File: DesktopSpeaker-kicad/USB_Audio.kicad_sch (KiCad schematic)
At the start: 20 parts, among them U2 PCM2902CDBR, Y170 12MHz

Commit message: Replace SWD header with TC2030-IDC and 4-pin header; set USB audio crystal caps and resistor parts
Co-Authored-By: Claude Sonnet 5.5 <noreply@anthropic.com>
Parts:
- C177, C178: value 22pF -> 33pF; LCSC C1653 -> C1663; MPN CL10C220JB8NNNC -> CL10C330JB8NNNC
- R170: LCSC (none) -> C112307
- R171, R172: LCSC (none) -> C107701

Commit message: Capture Source_Select_ADC sheet (PCM1862, 3V3_AUDIO LDO, codec load switch)
Co-Authored-By: Claude Sonnet 5.5 <noreply@anthropic.com>
Claude-Session: https://claude.ai/code/session_01N5RHheWSjDFDPbKVD5YVeJ
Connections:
- net 5V_LOGIC renamed 5V_CODEC
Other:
- note added: "Codec is powered only when CODEC_PWR_EN (U23) and 5V_LOGIC are on: D+ pull-up (R173 to VDDI) = USB attach. Do not enable CODEC_PWR_EN on DCP/unknown sources."
- note added: "Supply: 5V_CODEC (U23 load switch from 5V_LOGIC, 4.60-5.06 V worst case) feeds VBUS through 2.2R/1uF. DS range 4.35-5.25 V, 56 mA typ / 67 mA max, 250 uA suspend."
- note removed: "Codec is powered only when 5V_LOGIC_EN is high: D+ pull-up (R173 to VDDI) = USB attach. Do not enable on DCP/unknown sources."
- note removed: "Supply: 5V_LOGIC (U14 TPS63802, 4.60-5.06 V worst case) feeds VBUS through 2.2R/1uF. DS range 4.35-5.25 V, 56 mA typ / 67 mA max, 250 uA suspend."
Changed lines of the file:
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@@
 (wire (pts (xy 93.98 68.58) (xy 90.17 68.58)) (stroke (width 0) (type default)))
 (wire (pts (xy 82.55 68.58) (xy 57 68.58)) (stroke (width 0) (type default)))
-(hierarchical_label "5V_LOGIC" (shape input) (at 57 68.58 0) (effects (font (size 1.0 1.0)) (justify left bottom)))
+(hierarchical_label "5V_CODEC" (shape input) (at 57 68.58 0) (effects (font (size 1.0 1.0)) (justify left bottom)))
 (symbol (lib_id "PD_R:PD_R") (at 86.36 68.58 90) (unit 1) (exclude_from_sim no) (in_bom yes) (on_board yes) (dnp no) (property "Reference" "R170" (at 86.36 64.38 270) (effects (font (size 1.27 1.27)) )) (property "Value" "2.2" (at 86.36 65.98 270) (effects (font (size 1.27 1.27)) )) (property "Footprint" "DesktopSpeaker:PD_R_0603" (at 86.36 68.58 0) (hide yes) (effects (font (size 1.27 1.27)))) (property "MPN" "RC0603FR-072R2L" (at 86.36 68.58 0) (hide yes) (effects (font (size 1.27 1.27)))) (property "Manufacturer" "YAGEO" (at 86.36 68.58 0) (hide yes) (effects (font (size 1 1)))) (property "LCSC" "C112307" (at 86.36 68.58 0) (hide yes) (effects (font (size 1 1)))) (pin "1") (pin "2") (instances (project "DesktopSpeaker" (path "/feda53ed-537d-4f88-9436-c6075776255b/54e0bbc5-df7c-4047-acfa-4732ab128bc4" (reference "R170") (unit 1)))))
 (symbol (lib_id "PD_C:PD_C") (at 93.98 72.39 0) (unit 1) (exclude_from_sim no) (in_bom yes) (on_board yes) (dnp no) (property "Reference" "C170" (at 95.25 71.12 0) (effects (font (size 1.27 1.27)) (justify left))) (property "Value" "1uF" (at 95.25 73.66 0) (effects (font (size 1.27 1.27)) (justify left))) (property "Footprint" "DesktopSpeaker:PD_C_0805" (at 93.98 72.39 0) (hide yes) (effects (font (size 1.27 1.27)))) (property "MPN" "CL21B105KBFNNNE" (at 93.98 72.39 0) (hide yes) (effects (font (size 1.27 1.27)))) (property "Manufacturer" "Samsung Electro-Mechanics" (at 93.98 72.39 0) (hide yes) (effects (font (size 1 1)))) (property "LCSC" "C28323" (at 93.98 72.39 0) (hide yes) (effects (font (size 1 1)))) (pin "1") (pin "2") (instances (project "DesktopSpeaker" (path "/feda53ed-537d-4f88-9436-c6075776255b/54e0bbc5-df7c-4047-acfa-4732ab128bc4" (reference "C170") (unit 1)))))
@@
 (symbol (lib_id "power:GND") (at 180.34 137.16 0) (unit 1) (exclude_from_sim no) (in_bom no) (on_board no) (dnp no) (property "Reference" "#PWR713" (at 180.34 140.97 0) (effects (font (size 1.27 1.27)) (hide yes))) (property "Value" "GND" (at 180.34 142.24 0) (effects (font (size 1.27 1.27)) (hide yes))) (pin "1") (instances (project "DesktopSpeaker" (path "/feda53ed-537d-4f88-9436-c6075776255b/54e0bbc5-df7c-4047-acfa-4732ab128bc4" (reference "#PWR713") (unit 1)))))
 (hierarchical_label "USB_AUDIO_R" (shape output) (at 215.9 129.54 0) (effects (font (size 1.0 1.0)) (justify right bottom)))
-(text "Supply: 5V_LOGIC (U14 TPS63802, 4.60-5.06 V worst case) feeds VBUS through 2.2R/1uF. DS range 4.35-5.25 V, 56 mA typ / 67 mA max, 250 uA suspend." (at 57 53.6 0) (effects (font (size 1 1)) (justify left bottom)))
-(text "Codec is powered only when 5V_LOGIC_EN is high: D+ pull-up (R173 to VDDI) = USB attach. Do not enable on DCP/unknown sources." (at 57 56.1 0) (effects (font (size 1 1)) (justify left bottom)))
+(text "Supply: 5V_CODEC (U23 load switch from 5V_LOGIC, 4.60-5.06 V worst case) feeds VBUS through 2.2R/1uF. DS range 4.35-5.25 V, 56 mA typ / 67 mA max, 250 uA suspend." (at 57 53.6 0) (effects (font (size 1 1)) (justify left bottom)))
+(text "Codec is powered only when CODEC_PWR_EN (U23) and 5V_LOGIC are on: D+ pull-up (R173 to VDDI) = USB attach. Do not enable CODEC_PWR_EN on DCP/unknown sources." (at 57 56.1 0) (effects (font (size 1 1)) (justify left bottom)))
 (text "SEL0/SEL1 = high (VDDI). HID0-2, DIN, VINL/R unused. SSPND (suspend flag, active low) reserved for a later MCU input." (at 57 58.6 0) (effects (font (size 1 1)) (justify left bottom)))
 (text "USB_DP/USB_DN come from J1 via D1 (root). Later source-detect mux goes between those root nets and these ports." (at 57 61.1 0) (effects (font (size 1 1)) (justify left bottom)))

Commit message: Repackage passives to 0402/0805 hand-solder footprints; update BOM and flags
Co-Authored-By: Claude Sonnet 5.5 <noreply@anthropic.com>
Claude-Session: https://claude.ai/code/session_01N5RHheWSjDFDPbKVD5YVeJ
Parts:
- C170, C171, C172, C173, C174: footprint DesktopSpeaker:PD_C_0805 -> DesktopSpeaker:C_0402_1005Metric_Pad0.74x0.62mm_HandSolder; LCSC C28323 -> C29266; MPN CL21B105KBFNNNE -> CL05A105KO5NNNC
- C175, C176: footprint DesktopSpeaker:PD_C_0805 -> DesktopSpeaker:C_0805_2012Metric_Pad1.18x1.45mm_HandSolder
- C177, C178: footprint DesktopSpeaker:PD_C_0603 -> DesktopSpeaker:C_0402_1005Metric_Pad0.74x0.62mm_HandSolder; LCSC C1663 -> (none); MPN CL10C330JB8NNNC -> GRM1555C1H330JA01D; Manufacturer Samsung Electro-Mechanics -> Murata
- C186, C187: footprint DesktopSpeaker:PD_C_1206 -> DesktopSpeaker:C_0805_2012Metric_Pad1.18x1.45mm_HandSolder; LCSC C51205 -> (none); MPN CL31B475KBHNNNE -> CL21A475KAQNNNE
- R170: footprint DesktopSpeaker:PD_R_0603 -> DesktopSpeaker:R_0402_1005Metric_Pad0.72x0.64mm_HandSolder; LCSC C112307 -> (none); MPN RC0603FR-072R2L -> RC0402FR-072R2L; Manufacturer YAGEO -> Yageo
- R171, R172: footprint DesktopSpeaker:PD_R_0603 -> DesktopSpeaker:R_0402_1005Metric_Pad0.72x0.64mm_HandSolder; LCSC C107701 -> (none); MPN RC0603FR-0722RL -> RC0402FR-0722RL; Manufacturer YAGEO -> Yageo
- R173: footprint DesktopSpeaker:PD_R_0603 -> DesktopSpeaker:R_0402_1005Metric_Pad0.72x0.64mm_HandSolder; LCSC C114668 -> C114759; MPN RC0603FR-071K5L -> RC0402FR-071K5L; Manufacturer YAGEO -> Yageo
- R174: footprint DesktopSpeaker:PD_R_0603 -> DesktopSpeaker:R_0402_1005Metric_Pad0.72x0.64mm_HandSolder; LCSC C105578 -> (none); MPN RC0603FR-071ML -> RC0402FR-071ML; Manufacturer YAGEO -> Yageo
- R175, R176: footprint DesktopSpeaker:PD_R_0603 -> DesktopSpeaker:R_0402_1005Metric_Pad0.72x0.64mm_HandSolder; LCSC C14675 -> C60491; MPN RC0603FR-07100KL -> RC0402FR-07100KL; Manufacturer YAGEO -> Yageo

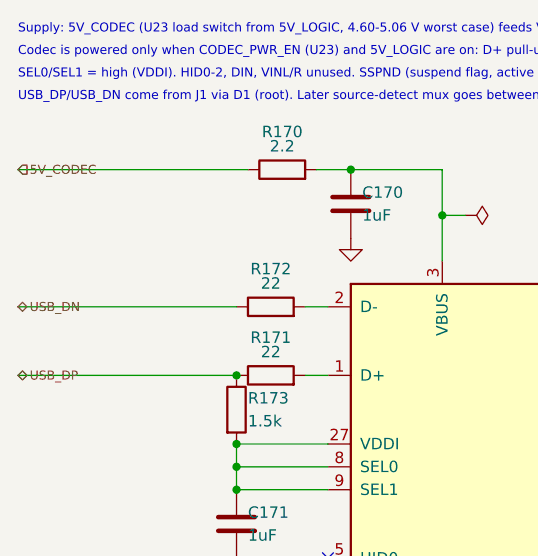
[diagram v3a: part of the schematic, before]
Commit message: Routing R6a-R6m adopted into project board; ERC cleanup, MCU pin swaps, C241 2.2uF, SW100 footprint fix, reviews and helpers
Co-Authored-By: Claude Sonnet 5.5 <noreply@anthropic.com>
Claude-Session: https://claude.ai/code/session_016fe4xPJbEE2SjGafuyNLjb
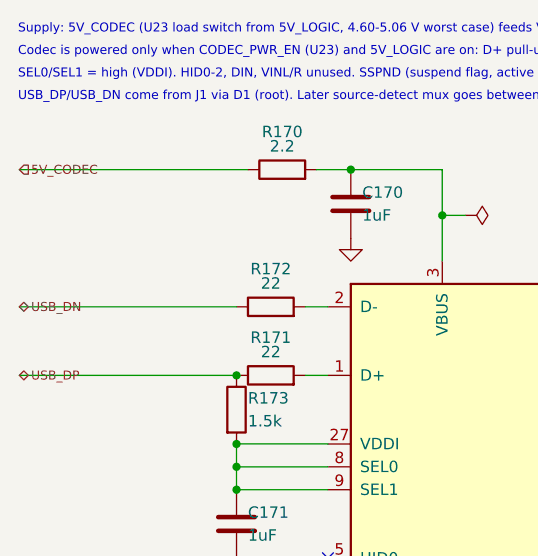
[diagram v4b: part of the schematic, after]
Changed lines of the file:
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@@
 (junction (at 93.98 68.58) (diameter 0) (color 0 0 0 0))
 (wire (pts (xy 93.98 68.58) (xy 90.17 68.58)) (stroke (width 0) (type default)))
-(wire (pts (xy 82.55 68.58) (xy 57 68.58)) (stroke (width 0) (type default)))
-(hierarchical_label "5V_CODEC" (shape input) (at 57 68.58 0) (effects (font (size 1.0 1.0)) (justify left bottom)))
+(wire (pts (xy 82.55 68.58) (xy 57.15 68.58)) (stroke (width 0) (type default)))
+(hierarchical_label "5V_CODEC" (shape input) (at 57.15 68.58 0) (effects (font (size 1.0 1.0)) (justify left bottom)))
 (symbol (lib_id "PD_R:PD_R") (at 86.36 68.58 90) (unit 1) (exclude_from_sim no) (in_bom yes) (on_board yes) (dnp no) (property "Reference" "R170" (at 86.36 64.38 270) (effects (font (size 1.27 1.27)) )) (property "Value" "2.2" (at 86.36 65.98 270) (effects (font (size 1.27 1.27)) )) (property "Footprint" "DesktopSpeaker:R_0402_1005Metric_Pad0.72x0.64mm_HandSolder" (at 86.36 68.58 0) (hide yes) (effects (font (size 1.27 1.27)))) (property "MPN" "RC0402FR-072R2L" (at 86.36 68.58 0) (hide yes) (effects (font (size 1.27 1.27)))) (property "Manufacturer" "Yageo" (at 86.36 68.58 0) (hide yes) (effects (font (size 1 1)))) (property "LCSC" "" (at 86.36 68.58 0) (hide yes) (effects (font (size 1 1)))) (pin "1") (pin "2") (instances (project "DesktopSpeaker" (path "/feda53ed-537d-4f88-9436-c6075776255b/54e0bbc5-df7c-4047-acfa-4732ab128bc4" (reference "R170") (unit 1)))))
 (symbol (lib_id "PD_C:PD_C") (at 93.98 72.39 0) (unit 1) (exclude_from_sim no) (in_bom yes) (on_board yes) (dnp no) (property "Reference" "C170" (at 95.25 71.12 0) (effects (font (size 1.27 1.27)) (justify left))) (property "Value" "1uF" (at 95.25 73.66 0) (effects (font (size 1.27 1.27)) (justify left))) (property "Footprint" "DesktopSpeaker:C_0402_1005Metric_Pad0.74x0.62mm_HandSolder" (at 93.98 72.39 0) (hide yes) (effects (font (size 1.27 1.27)))) (property "MPN" "CL05A105KO5NNNC" (at 93.98 72.39 0) (hide yes) (effects (font (size 1.27 1.27)))) (property "Manufacturer" "Samsung Electro-Mechanics" (at 93.98 72.39 0) (hide yes) (effects (font (size 1 1)))) (property "LCSC" "C29266" (at 93.98 72.39 0) (hide yes) (effects (font (size 1 1)))) (pin "1") (pin "2") (instances (project "DesktopSpeaker" (path "/feda53ed-537d-4f88-9436-c6075776255b/54e0bbc5-df7c-4047-acfa-4732ab128bc4" (reference "C170") (unit 1)))))
 (symbol (lib_id "power:GND") (at 93.98 76.2 0) (unit 1) (exclude_from_sim no) (in_bom no) (on_board no) (dnp no) (property "Reference" "#PWR701" (at 93.98 80.01 0) (effects (font (size 1.27 1.27)) (hide yes))) (property "Value" "GND" (at 93.98 81.28 0) (effects (font (size 1.27 1.27)) (hide yes))) (pin "1") (instances (project "DesktopSpeaker" (path "/feda53ed-537d-4f88-9436-c6075776255b/54e0bbc5-df7c-4047-acfa-4732ab128bc4" (reference "#PWR701") (unit 1)))))
 (wire (pts (xy 91.44 83.82) (xy 88.9 83.82)) (stroke (width 0) (type default)))
-(wire (pts (xy 81.28 83.82) (xy 57 83.82)) (stroke (width 0) (type default)))
+(wire (pts (xy 81.28 83.82) (xy 57.15 83.82)) (stroke (width 0) (type default)))
 (wire (pts (xy 91.44 91.44) (xy 88.9 91.44)) (stroke (width 0) (type default)))
-(wire (pts (xy 81.28 91.44) (xy 57 91.44)) (stroke (width 0) (type default)))
+(wire (pts (xy 81.28 91.44) (xy 57.15 91.44)) (stroke (width 0) (type default)))
 (symbol (lib_id "PD_R:PD_R") (at 85.09 83.82 90) (unit 1) (exclude_from_sim no) (in_bom yes) (on_board yes) (dnp no) (property "Reference" "R172" (at 85.09 79.62 270) (effects (font (size 1.27 1.27)) )) (property "Value" "22" (at 85.09 81.22 270) (effects (font (size 1.27 1.27)) )) (property "Footprint" "DesktopSpeaker:R_0402_1005Metric_Pad0.72x0.64mm_HandSolder" (at 85.09 83.82 0) (hide yes) (effects (font (size 1.27 1.27)))) (property "MPN" "RC0402FR-0722RL" (at 85.09 83.82 0) (hide yes) (effects (font (size 1.27 1.27)))) (property "Manufacturer" "Yageo" (at 85.09 83.82 0) (hide yes) (effects (font (size 1 1)))) (property "LCSC" "" (at 85.09 83.82 0) (hide yes) (effects (font (size 1 1)))) (pin "1") (pin "2") (instances (project "DesktopSpeaker" (path "/feda53ed-537d-4f88-9436-c6075776255b/54e0bbc5-df7c-4047-acfa-4732ab128bc4" (reference "R172") (unit 1)))))
 (symbol (lib_id "PD_R:PD_R") (at 85.09 91.44 90) (unit 1) (exclude_from_sim no) (in_bom yes) (on_board yes) (dnp no) (property "Reference" "R171" (at 85.09 87.24 270) (effects (font (size 1.27 1.27)) )) (property "Value" "22" (at 85.09 88.84 270) (effects (font (size 1.27 1.27)) )) (property "Footprint" "DesktopSpeaker:R_0402_1005Metric_Pad0.72x0.64mm_HandSolder" (at 85.09 91.44 0) (hide yes) (effects (font (size 1.27 1.27)))) (property "MPN" "RC0402FR-0722RL" (at 85.09 91.44 0) (hide yes) (effects (font (size 1.27 1.27)))) (property "Manufacturer" "Yageo" (at 85.09 91.44 0) (hide yes) (effects (font (size 1 1)))) (property "LCSC" "" (at 85.09 91.44 0) (hide yes) (effects (font (size 1 1)))) (pin "1") (pin "2") (instances (project "DesktopSpeaker" (path "/feda53ed-537d-4f88-9436-c6075776255b/54e0bbc5-df7c-4047-acfa-4732ab128bc4" (reference "R171") (unit 1)))))
-(hierarchical_label "USB_DN" (shape bidirectional) (at 57 83.82 0) (effects (font (size 1.0 1.0)) (justify left bottom)))
-(hierarchical_label "USB_DP" (shape bidirectional) (at 57 91.44 0) (effects (font (size 1.0 1.0)) (justify left bottom)))
+(hierarchical_label "USB_DN" (shape bidirectional) (at 57.15 83.82 0) (effects (font (size 1.0 1.0)) (justify left bottom)))
+(hierarchical_label "USB_DP" (shape bidirectional) (at 57.15 91.44 0) (effects (font (size 1.0 1.0)) (justify left bottom)))
 (junction (at 81.28 91.44) (diameter 0) (color 0 0 0 0))
 (symbol (lib_id "PD_R:PD_R") (at 81.28 95.25 0) (unit 1) (exclude_from_sim no) (in_bom yes) (on_board yes) (dnp no) (property "Reference" "R173" (at 82.55 93.98 0) (effects (font (size 1.27 1.27)) (justify left))) (property "Value" "1.5k" (at 82.55 96.52 0) (effects (font (size 1.27 1.27)) (justify left))) (property "Footprint" "DesktopSpeaker:R_0402_1005Metric_Pad0.72x0.64mm_HandSolder" (at 81.28 95.25 0) (hide yes) (effects (font (size 1.27 1.27)))) (property "MPN" "RC0402FR-071K5L" (at 81.28 95.25 0) (hide yes) (effects (font (size 1.27 1.27)))) (property "Manufacturer" "Yageo" (at 81.28 95.25 0) (hide yes) (effects (font (size 1 1)))) (property "LCSC" "C114759" (at 81.28 95.25 0) (hide yes) (effects (font (size 1 1)))) (pin "1") (pin "2") (instances (project "DesktopSpeaker" (path "/feda53ed-537d-4f88-9436-c6075776255b/54e0bbc5-df7c-4047-acfa-4732ab128bc4" (reference "R173") (unit 1)))))

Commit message: Y200 24.576 MHz crystal with 15 pF load caps, C275 3D model, schematic/PCB sourcing fields synced to BOM
Co-Authored-By: Claude Sonnet 5.5 <noreply@anthropic.com>
Claude-Session: https://claude.ai/code/session_016fe4xPJbEE2SjGafuyNLjb
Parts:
- C177, C178: LCSC (none) -> C5137486; MPN GRM1555C1H330JA01D -> FCC0402N330J500AT; Manufacturer Murata -> FOJAN
- C186, C187: LCSC (none) -> C1779
- R170: LCSC (none) -> C327251
- R171, R172: LCSC (none) -> C114765
- R174: LCSC (none) -> C138033
- Y170: LCSC C9002 -> C368730; MPN X322512MSB4SI -> K3A120002010; Manufacturer YXC -> KYX
